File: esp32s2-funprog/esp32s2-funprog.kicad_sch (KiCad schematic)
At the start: 49 parts, among them J1 OPGM, J2 PGM, J3 USB_C_Receptacle_USB2.0, J4 MOUNT, J5 MOUNT, Q1 SE4625-PandN, Q2 SE4625-PandN, SW1 TS-1187A-B-A-B, U1 ESP32-S2, U2 AP1117-33, Y1 40MHz

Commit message: Update design per print.
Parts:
- removed D1, D2, D3: WS2816C-2121, cnhardware:WS2816-2121, symbol WS2816C:WS2816C-2121
- added D1, D2, D3: XL-1010RGBC-WS2812B, cnhardware:XL-1010RGBC-WS812B, symbol cnhardware:SK6805-EC15
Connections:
- net GND: now also D1.4 (GND), D2.4 (GND), D3.4 (GND)
- net VDD: now also D1.2 (VDD), D2.2 (VDD), D3.2 (VDD)
- net WSO: now also D1.1 (DI)
- new net: D1.3 (DO), D2.1 (DI)
- new net: D2.3 (DO), D3.1 (DI)

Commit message: Tweaks
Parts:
- added D5, D6, D7, D8, D9: XL-1010RGBC-WS2812B, cnhardware:XL-1010RGBC-WS812B, symbol cnhardware:SK6805-EC15
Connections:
- net GND: now also D5.4 (GND), D6.4 (GND), D7.4 (GND), D8.4 (GND), D9.4 (GND)
- net VDD: now also D5.2 (VDD), D6.2 (VDD), D7.2 (VDD), D8.2 (VDD), D9.2 (VDD)
- net at D3.3 (DO): now also D5.1 (DI)
- new net: D5.3 (DO), D6.1 (DI)
- new net: D6.3 (DO), D7.1 (DI)
- new net: D7.3 (DO), D8.1 (DI)
- new net: D8.3 (DO), D9.1 (DI)
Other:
- moved on the sheet: D1, D2, D3

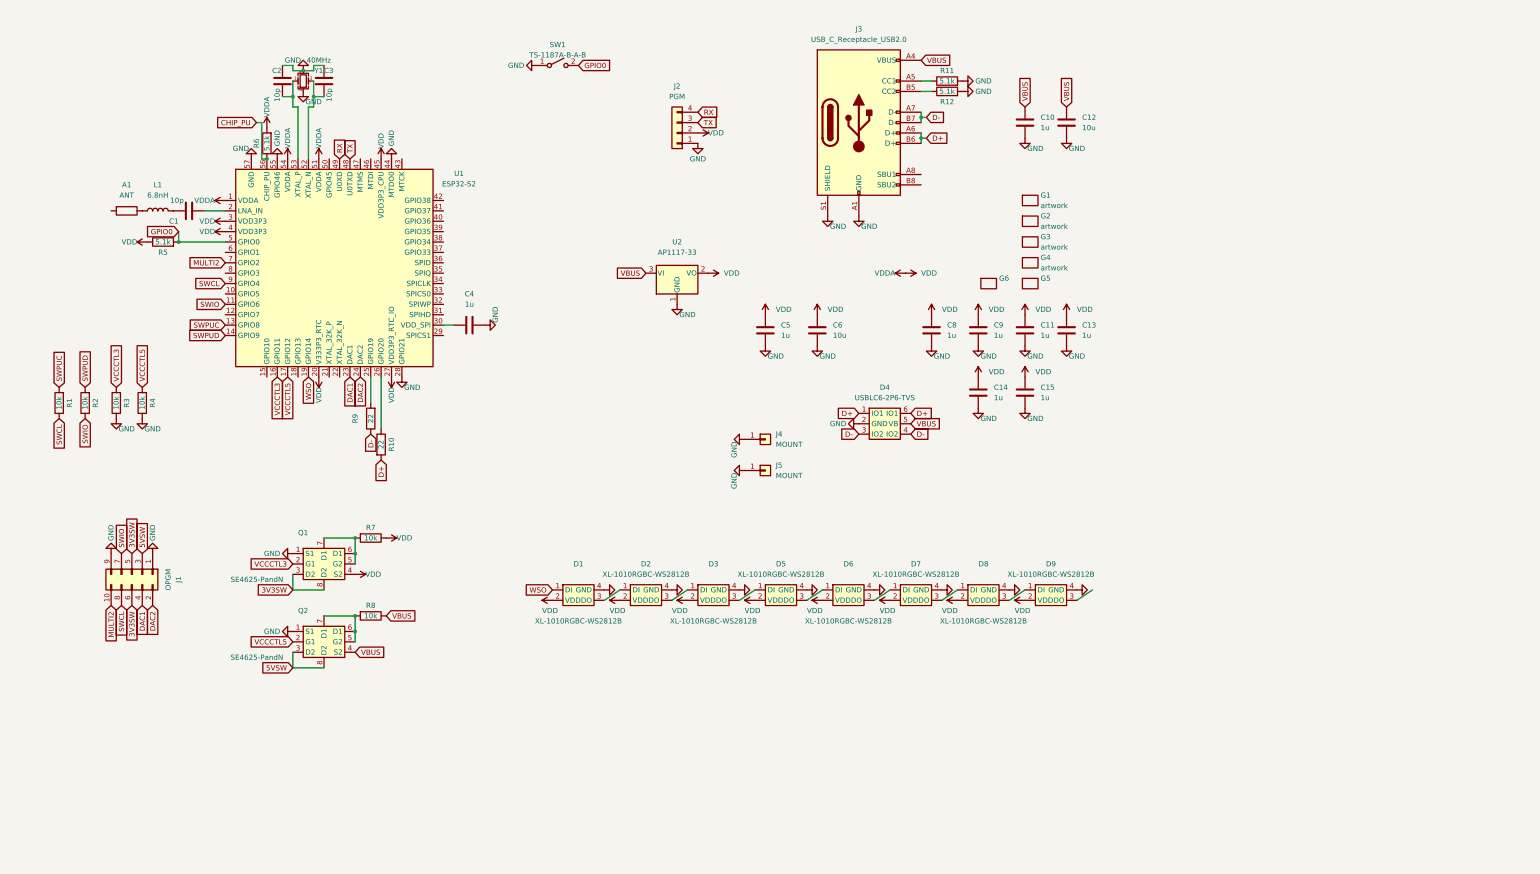
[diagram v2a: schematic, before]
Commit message: Maybe we can shoehorn it into the old programmer
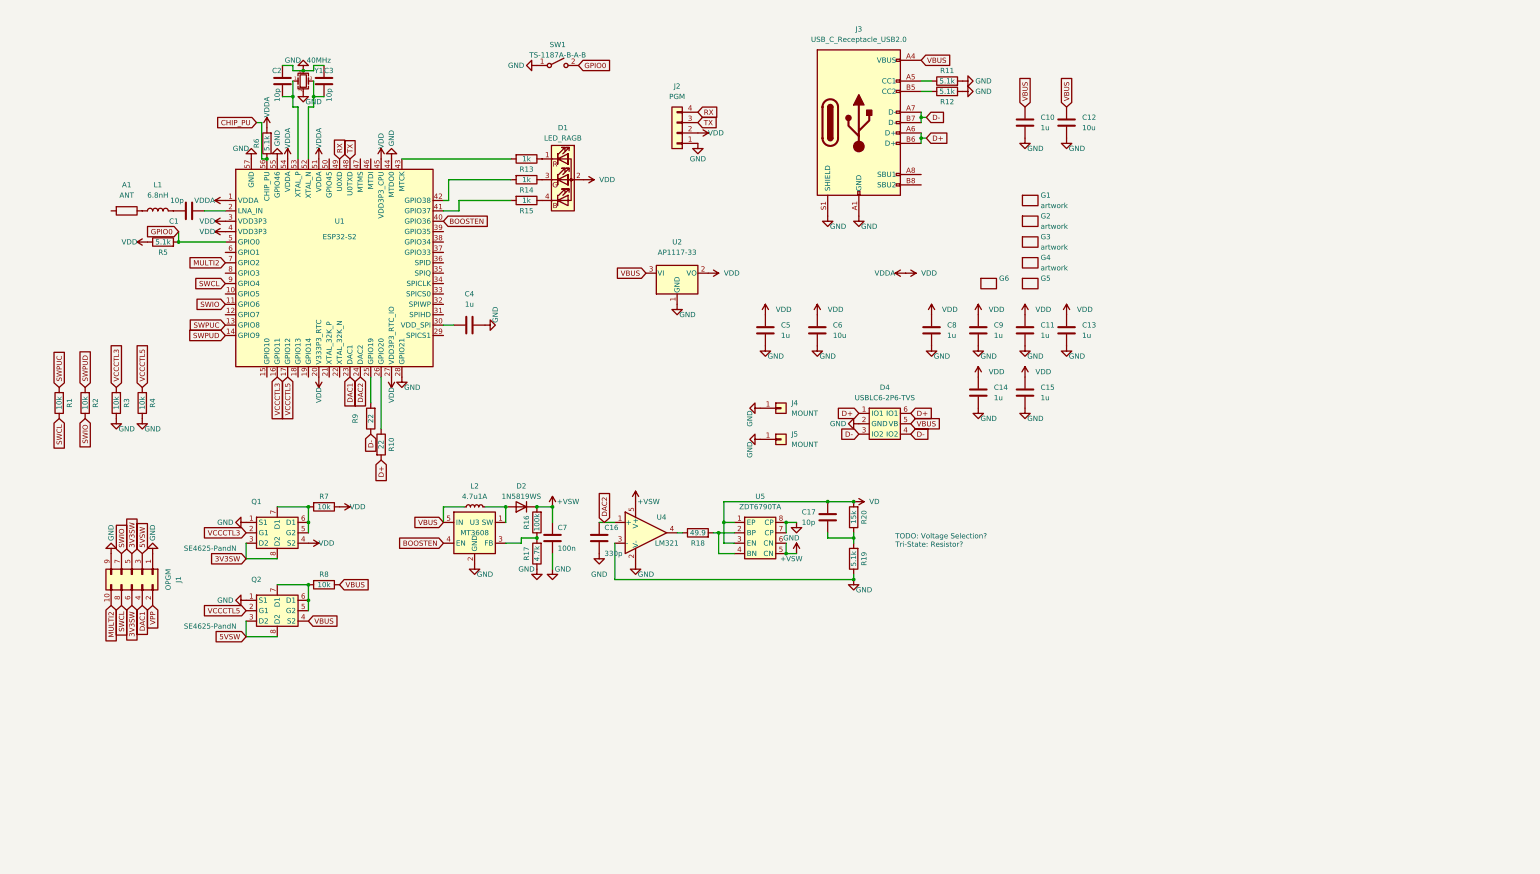
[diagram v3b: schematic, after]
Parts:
- removed D1, D2, D3, D5, D6, D7, D8, D9: XL-1010RGBC-WS2812B, cnhardware:XL-1010RGBC-WS812B, symbol cnhardware:SK6805-EC15
- added C16: 330p, Capacitor_SMD:C_0402_1005Metric, symbol Device:C
- added C17: 10p, Capacitor_SMD:C_0402_1005Metric, symbol Device:C
- added C7: 100n, Capacitor_SMD:C_0402_1005Metric, symbol Device:C
- added D1: LED_RAGB, LED_SMD:LED_WS2812B-2020_PLCC4_2.0x2.0mm, symbol Device:LED_RAGB
- added D2: 1N5819WS, Diode_SMD:D_SOD-323, symbol Device:D
- added L2: 4.7u1A, Inductor_SMD:L_1008_2520Metric, symbol Device:L_Small
- added R13, R14, R15: 1k, Resistor_SMD:R_0402_1005Metric, symbol Device:R
- added R16: 100k, Resistor_SMD:R_0402_1005Metric, symbol Device:R
- added R17: 4.7k, Resistor_SMD:R_0402_1005Metric, symbol Device:R
- added R18: 49.9, Resistor_SMD:R_0402_1005Metric, symbol Device:R
- added R19: 5.1k, Resistor_SMD:R_0402_1005Metric, symbol Device:R
- added R20: 15k, Resistor_SMD:R_0402_1005Metric, symbol Device:R
- added U3: MT3608, Package_TO_SOT_SMD:SOT-23-6, symbol Regulator_Switching:MT3608
- added U4: LM321, Package_TO_SOT_SMD:SOT-23-5, symbol Amplifier_Operational:LM321
- added U5: ZDT6790TA, Package_TO_SOT_SMD:SOT-223-8, symbol cnhardware:ZDT6790-COMPLEMENTARY-BJT
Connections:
- net DAC2: now also C16.1, U4.1 (+); no longer J1.2 (Pin_2)
- net GND: now also C16.2, C7.2, R17.1, R19.1, U3.2 (GND), U4.2 (V-), U4.3 (-), U5.7 (CP), U5.8 (CP)
- net VBUS: now also L2.1, U3.5 (IN)
- net VDD: now also D1.2 (A)
- net BOOSTEN: now reaches U1.40 (GPIO36)
- net BOOSTEN: now also U3.4 (EN)
- net at U1.41 (GPIO37): now also R15.2
- net at U1.42 (GPIO38): now also R14.2
- net at U1.43 (MTCK): now also R13.2
- net WSO: no longer names the net of U1.19 (GPIO14)
- new net: D2.2 (A), L2.2, U3.1 (SW)
- new net: C17.2, R19.2, R20.1
- new net: R16.1, R17.2, U3.3 (FB)
- new net: R18.1, U4.4
- new net: R18.2, U5.2 (BP), U5.4 (BN)
- new net: D1.1 (RK), R13.1
- new net: D1.3 (GK), R14.1
- new net: D1.4 (BK), R15.1
- new net +VSW: C7.1, D2.1 (K), R16.2, U4.5 (V+), U5.5 (CN), U5.6 (CN)
- new net VD: C17.1, R20.2, U5.1 (EP), U5.3 (EN)
- new net VPP: J1.2 (Pin_2)
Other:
- note added: "TODO: Voltage Selection? Tri-State: Resistor?"
- moved on the sheet: J4, J5, Q1, Q2, R7, R8

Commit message: Update design
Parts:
- added Q3: DWL336C, Package_TO_SOT_SMD:SOT-23-6, symbol cnhardware:DWL336C-P-AND-N
- added Q4, Q5: MOT2302, Package_TO_SOT_SMD:SOT-23, symbol Device:Q_NMOS_GDS
- added R21, R22: 10k, Resistor_SMD:R_0402_1005Metric, symbol Device:R
- added U6: COS4514, Package_TO_SOT_SMD:SOT-23-5, symbol cnhardware:COS4514-MUX-SPST
- added U8: HP3000, Package_DFN_QFN:DFN-8-1EP_2x2mm_P0.5mm_EP0.6x1.2mm, symbol cnhardware:HP3000-AD000-HD08R-DUAL-LOW-DRIVER
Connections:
- net +VSW: now also U6.5 (V+), U8.1 (ENA), U8.6 (VDD), U8.8 (ENB)
- net GND: now also Q3.5 (S1), Q4.3 (S), U6.3 (GND), U8.3 (GND), U8.9 (GND)
- net VD: now also Q3.2 (S2), Q5.2 (D), R21.1
- net VPP: now also Q3.4 (D2), Q3.6 (D1), Q5.3 (S), R22.2, U6.1 (COM)
- new net: Q3.3 (G2), U8.5 (OUTB)
- new net: Q3.1 (G1), U8.7 (OUTA)
- new net: Q4.2 (D), R22.1
- new net: R21.2, U6.2 (NO)
- new net VPPN2E: Q5.1 (G)
- new net VPPNEN: U8.2 (INA)
- new net VPPPD: Q4.1 (G)
- new net VPPPEN: U8.4 (INB)
- new net VPPUEN: U6.4 (IN)
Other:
- note added: "TODO: Primitive current monitoring? TODO: What if I want to drive output at very low voltages? Below VGSon for P fet in DWL, like 1.5V? No? Maybe another N fet?"
- moved on the sheet: R19, R20

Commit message: update with rev
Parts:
- removed Q5: MOT2302, Package_TO_SOT_SMD:SOT-23, symbol Device:Q_NMOS_GDS
- removed U2: AP1117-33, Package_TO_SOT_SMD:SOT-223-3_TabPin2, symbol Regulator_Linear:AP1117-33
- removed U4: LM321, Package_TO_SOT_SMD:SOT-23-5, symbol Amplifier_Operational:LM321
- removed U5: ZDT6790TA, Package_TO_SOT_SMD:SOT-223-8, symbol cnhardware:ZDT6790-COMPLEMENTARY-BJT
- removed U6: COS4514, Package_TO_SOT_SMD:SOT-23-5, symbol cnhardware:COS4514-MUX-SPST
- added C18, C22: 100n, Capacitor_SMD:C_0402_1005Metric, symbol Device:C
- added C19: 330p, Capacitor_SMD:C_0402_1005Metric, symbol Device:C
- added C20, C21, C23, C24: 10p, Capacitor_SMD:C_0402_1005Metric, symbol Device:C
- added C25: 10u, Capacitor_SMD:C_0603_1608Metric, symbol Device:C
- added C26: 1u, Capacitor_SMD:C_0402_1005Metric, symbol Device:C
- added Q6: 2N7002KDW, Package_TO_SOT_SMD:SOT-363_SC-70-6, symbol cnhardware:DWL336C-P-AND-N
- added Q7: MOT2302, Package_TO_SOT_SMD:SOT-23, symbol Device:Q_NMOS_GDS
- added R23: 12k, Resistor_SMD:R_0402_1005Metric, symbol Device:R
- added R24: 2.2k, Resistor_SMD:R_0402_1005Metric, symbol Device:R
- added R25: 49.9, Resistor_SMD:R_0402_1005Metric, symbol Device:R
- added R26: 15k, Resistor_SMD:R_0402_1005Metric, symbol Device:R
- added R27: 5.1k, Resistor_SMD:R_0402_1005Metric, symbol Device:R
- added R28, R29, R30, R31: 10k, Resistor_SMD:R_0402_1005Metric, symbol Device:R
- added U10: LM321, Package_TO_SOT_SMD:SOT-23-5, symbol Amplifier_Operational:LM321
- added U11: ZDT6790TA, Package_TO_SOT_SMD:SOT-223-8, symbol cnhardware:ZDT6790-COMPLEMENTARY-BJT
- added U12: COS4514, Package_TO_SOT_SMD:SOT-23-5, symbol cnhardware:COS4514-MUX-SPST
- added U13: ~, Package_DFN_QFN:DFN-8-1EP_3x3mm_P0.5mm_EP1.65x2.38mm, symbol cnhardware:NCP81155-GATE-DRIVER
- added U14, U15, U16, U9: AT8837, Package_DFN_QFN:DFN-8-1EP_2x2mm_P0.45mm_EP0.64x1.38mm, symbol cnhardware:BDR6122TC-MOTOR-DRIVER
- added U2, U4, U6: XC6206P332, Package_TO_SOT_SMD:SOT-23, symbol Regulator_Linear:IFX27001TFV26
- added U5: COSNE5532, Package_SO:MSOP-8_3x3mm_P0.65mm, symbol cnhardware:LM2903-SOIC8
- C14, C15: value 1u -> 10p; LCSC C106254 -> C106199
- C16: value 330p -> 1u; LCSC C13533 -> C106254
- C2, C3: value 10p -> 2.2p; LCSC C106199 -> C1559
- L2: value 4.7u1A -> 4.7u500mA; footprint Inductor_SMD:L_1008_2520Metric -> Inductor_SMD:L_0805_2012Metric; LCSC C98340 -> C63166
- Q3, U8: now not fitted; now left out of the parts list
- Q4: value MOT2302 -> 2N7002; LCSC C5143129 -> C8545
- R13, R14, R15: value 1k -> 510; LCSC C102748 -> C25123
- R16: value 100k -> 510; LCSC C25741 -> C25123
- R17: value 4.7k -> 2.2k; LCSC C25900 -> C25879
- R18: value 49.9 -> 2.2k; LCSC C25120 -> C25879
- R19: value 5.1k -> 15k; LCSC C105872 -> C25756
- R20: value 15k -> 5.1k; LCSC C25756 -> C105872
- R21: value 10k -> 15k; LCSC C144807 -> C25756
- R22: value 10k -> 5.1k; LCSC C144807 -> C105872
- U3: footprint Package_TO_SOT_SMD:SOT-23-6 -> Package_TO_SOT_SMD:SOT-23-5
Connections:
- net +VSW: now also C25.1, R23.2, U10.5 (V+), U11.5 (CN), U11.6 (CN), U12.5 (V+), U13.1 (BST), U15.1 (VM), U16.1 (VM), U5.8 (Vcc); no longer R16.2
- net 3V3SW: no longer J1.6 (Pin_6)
- net BOOSTEN: now also U1.43 (MTCK); no longer U1.40 (GPIO36)
- net DAC1: now also C14.2, C19.1, U10.1 (+), U5.3 (I1+); no longer J1.4 (Pin_4)
- net DAC2: now also C15.2, U5.5 (I2+); no longer C16.1
- net GND: now also C14.1, C15.1, R16.1, R20.1, R22.1, C18.2, C19.2, C22.2, C23.2, C24.2, C25.2, C26.1, Q6.4 (D2), Q7.3 (S), R27.1, U10.2 (V-), U11.7 (CP), U11.8 (CP), U12.3 (GND), U13.6 (GND), U13.9 (GND), U14.4 (GND), U14.9 (FLAG), U15.4 (GND), U15.9 (FLAG), U16.4 (GND), U16.9 (FLAG), U2.1 (GND), U4.1 (GND), U5.4 (GND), U6.1 (GND), U9.4 (GND), U9.9 (FLAG); no longer C14.2, C15.2, R17.1, R19.1
- net MULTI2: now also J1.6 (Pin_6); no longer J1.10 (Pin_10)
- net VBUS: now also C26.2, U13.4 (VCC), U2.3 (I), U4.3 (I), U6.3 (I)
- net VCCCTL3: now also U1.10 (GPIO5); no longer U1.16 (GPIO11)
- net VCCCTL5: now also U1.8 (GPIO3); no longer U1.17 (GPIO12)
- net VD: now also Q6.6 (D1), R28.1; no longer C17.1, R20.2, R21.1
- net VDD: now also R18.1, U14.6 (IN1), U14.8 (VCC), U15.6 (IN1), U15.8 (VCC), U16.6 (IN1), U16.8 (VCC), U4.2 (Q), U9.6 (IN1), U9.8 (VCC); no longer C14.1, C15.1, Q1.4 (S2), R7.1, U1.20 (V333P3_RTC)
- net VPP: now also U12.1 (COM); no longer J1.2 (Pin_2), R22.2
- net VPI1: now reaches Q4.2 (D)
- net VPI1: now also R18.2, U1.19 (GPIO14); no longer R22.1
- net at R17.2, U3.3 (FB): now also R16.2, R23.1; no longer R16.1
- net VD2: now reaches R21.2
- net VD2: now also J1.4 (Pin_4), C21.1, C23.1, U5.7 (O2)
- net OPEN1: now reaches U1.18 (GPIO13)
- net OPEN1: now also U14.7 (nSLP)
- net at R15.2: now also D1.4 (BK); no longer U1.41 (GPIO37)
- net at R14.2: now also D1.3 (GK); no longer U1.42 (GPIO38)
- net at R13.2: now also D1.1 (RK); no longer U1.43 (MTCK)
- net at U1.46 (MTDI): now also R14.1
- net at U1.47 (MTMS): now also R15.1
- net at U1.50 (GPIO45): now also R13.1
- net MULTI1: now reaches U1.6 (GPIO1)
- net MULTI1: now also J1.10 (Pin_10)
- net VPPNEN: no longer names the net of U8.2 (INA)
- net VPPPD renamed VPP1
- net VPP1: now also J1.2 (Pin_2), Q6.2 (S2), Q6.5 (S1), R29.2, R30.2, U13.7 (SW), U9.2 (OUT1)
- net VPPPEN: no longer names the net of U8.4 (INB)
- new net: R30.1, U14.2 (OUT1)
- new net: Q1.4 (S2), R7.1, U6.2 (Q)
- new net: Q7.2 (D), R29.1
- new net: C20.2, R26.1, R27.2, U10.3 (-)
- new net: R31.1, U16.2 (OUT1)
- new net: R25.2, U11.2 (BP), U11.4 (BN)
- new net: R28.2, U12.2 (NO)
- new net: Q6.3 (G2), U13.5 (DL)
- new net: Q6.1 (G1), U13.8 (DH)
- new net: C18.1, R17.1, R24.1
- new net: R25.1, U10.4
- new net BOOSTV: R24.2, U1.42 (GPIO38)
- new net D1OEN: U13.3 (EN)
- new net D1OV: U13.2 (PWM)
- new net D1PDEN: Q7.1 (G)
- new net D1PUEN: U12.4 (IN)
- new net OD1: U1.16 (GPIO11), U14.5 (IN2), U9.5 (IN2)
- new net OD2: U15.5 (IN2), U16.5 (IN2)
- new net OEN1: U1.17 (GPIO12), U9.7 (nSLP)
- new net OEN2: U15.7 (nSLP)
- new net OPEN2: U16.7 (nSLP)
- new net V1FB: C17.2, R19.1, R20.2, U5.2 (I1-)
- new net V2FB: C21.2, R21.1, R22.2, U5.6 (I2-)
- new net VD1: C17.1, C20.1, C22.1, C24.1, R19.2, R26.2, U11.1 (EP), U11.3 (EN), U14.1 (VM), U5.1 (O1), U9.1 (VM)
- new net VDDA: C16.1, U1.20 (V333P3_RTC), U2.2 (Q)
- new net VPP2: R31.2, U15.2 (OUT1)
- no-connect marks 0 -> 4
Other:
- note added: "+VST may be 7.5 to 16.6V"
- note added: "TODO: Evaluate C14/C15, C17, C21 C2, C3"
- note removed: "TODO: Voltage Selection? Tri-State: Resistor?"
- moved on the sheet: C11, C13, C5, C6, C7, C8, C9, D2, D4, G6, J1, J3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

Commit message: Update fixing 6-pin pinout
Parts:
- U3: footprint Package_TO_SOT_SMD:SOT-23-5 -> Package_TO_SOT_SMD:SOT-23-6
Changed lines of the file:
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@@
       (effects (font (size 1.27 1.27)))
     )
-    (property "Footprint" "Package_TO_SOT_SMD:SOT-23-5" (at 149.86 149.86 0)
+    (property "Footprint" "Package_TO_SOT_SMD:SOT-23-6" (at 149.86 149.86 0)
       (effects (font (size 1.27 1.27) italic) (justify left) hide)
     )

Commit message: Bump - back to legacy
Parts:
- removed C16, C26: 1u, Capacitor_SMD:C_0402_1005Metric, symbol Device:C
- removed C17, C20, C21, C23, C24: 10p, Capacitor_SMD:C_0402_1005Metric, symbol Device:C
- removed C18, C22, C7: 100n, Capacitor_SMD:C_0402_1005Metric, symbol Device:C
- removed C19: 330p, Capacitor_SMD:C_0402_1005Metric, symbol Device:C
- removed C25: 10u, Capacitor_SMD:C_0603_1608Metric, symbol Device:C
- removed D1: LED_RAGB, LED_SMD:LED_WS2812B-2020_PLCC4_2.0x2.0mm, symbol Device:LED_RAGB
- removed D2: 1N5819WS, Diode_SMD:D_SOD-323, symbol Device:D
- removed L2: 4.7u500mA, Inductor_SMD:L_0805_2012Metric, symbol Device:L_Small
- removed Q3: DWL336C, Package_TO_SOT_SMD:SOT-23-6, symbol cnhardware:DWL336C-P-AND-N
- removed Q4: 2N7002, Package_TO_SOT_SMD:SOT-23, symbol Device:Q_NMOS_GDS
- removed Q6: 2N7002KDW, Package_TO_SOT_SMD:SOT-363_SC-70-6, symbol cnhardware:DWL336C-P-AND-N
- removed Q7: MOT2302, Package_TO_SOT_SMD:SOT-23, symbol Device:Q_NMOS_GDS
- removed R13, R14, R15, R16: 510, Resistor_SMD:R_0402_1005Metric, symbol Device:R
- removed R17, R18, R24: 2.2k, Resistor_SMD:R_0402_1005Metric, symbol Device:R
- removed R19, R21, R26: 15k, Resistor_SMD:R_0402_1005Metric, symbol Device:R
- removed R20, R22, R27: 5.1k, Resistor_SMD:R_0402_1005Metric, symbol Device:R
- removed R23: 12k, Resistor_SMD:R_0402_1005Metric, symbol Device:R
- removed R25: 49.9, Resistor_SMD:R_0402_1005Metric, symbol Device:R
- removed R28, R29, R30, R31: 10k, Resistor_SMD:R_0402_1005Metric, symbol Device:R
- removed U10: LM321, Package_TO_SOT_SMD:SOT-23-5, symbol Amplifier_Operational:LM321
- removed U11: ZDT6790TA, Package_TO_SOT_SMD:SOT-223-8, symbol cnhardware:ZDT6790-COMPLEMENTARY-BJT
- removed U12: COS4514, Package_TO_SOT_SMD:SOT-23-5, symbol cnhardware:COS4514-MUX-SPST
- removed U13: ~, Package_DFN_QFN:DFN-8-1EP_3x3mm_P0.5mm_EP1.65x2.38mm, symbol cnhardware:NCP81155-GATE-DRIVER
- removed U14, U15, U16, U9: AT8837, Package_DFN_QFN:DFN-8-1EP_2x2mm_P0.45mm_EP0.64x1.38mm, symbol cnhardware:BDR6122TC-MOTOR-DRIVER
- removed U2, U4, U6: XC6206P332, Package_TO_SOT_SMD:SOT-23, symbol Regulator_Linear:IFX27001TFV26
- removed U3: MT3608, Package_TO_SOT_SMD:SOT-23-6, symbol Regulator_Switching:MT3608
- removed U5: COSNE5532, Package_SO:MSOP-8_3x3mm_P0.65mm, symbol cnhardware:LM2903-SOIC8
- removed U8: HP3000, Package_DFN_QFN:DFN-8-1EP_2x2mm_P0.5mm_EP0.6x1.2mm, symbol cnhardware:HP3000-AD000-HD08R-DUAL-LOW-DRIVER
- added D1, D2, D3, D5, D6, D7, D8, D9: XL-1010RGBC-WS2812B, cnhardware:XL-1010RGBC-WS812B, symbol cnhardware:SK6805-EC15
- added U2: AP1117-33, Package_TO_SOT_SMD:SOT-223-3_TabPin2, symbol Regulator_Linear:AP1117-33
- C14, C15: value 10p -> 1u; LCSC C106199 -> C106254
- C2, C3: value 2.2p -> 10p; LCSC C1559 -> C106199
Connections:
- net OD1 is gone; now on net VCCCTL3: U1.16 (GPIO11)
- net OEN1 is gone; now on net VCCCTL5: U1.17 (GPIO12)
- net VD2 is gone; now on net DAC1: J1.4 (Pin_4)
- net VDDA is gone; now on net VDD: U1.20 (V333P3_RTC)
- net VPP1 is gone; now on net DAC2: J1.2 (Pin_2)
- net 3V3SW: now also J1.6 (Pin_6)
- net DAC1: no longer C14.2
- net DAC2: no longer C15.2
- net GND: now also C14.2, C15.2, D1.4 (GND), D2.4 (GND), D3.4 (GND), D5.4 (GND), D6.4 (GND), D7.4 (GND), D8.4 (GND), D9.4 (GND), U2.1 (GND); no longer C14.1, C15.1
- net MULTI2: now also J1.10 (Pin_10); no longer J1.6 (Pin_6)
- net VBUS: now also U2.3 (VI)
- net VCCCTL3: no longer U1.10 (GPIO5)
- net VCCCTL5: no longer U1.8 (GPIO3)
- net VDD: now also C14.1, C15.1, Q1.4 (S2), R7.1, D1.2 (VDD), D2.2 (VDD), D3.2 (VDD), D5.2 (VDD), D6.2 (VDD), D7.2 (VDD), D8.2 (VDD), D9.2 (VDD), U2.2 (VO)
- net BOOSTEN: no longer names the net of U1.43 (MTCK)
- net BOOSTV: no longer names the net of U1.42 (GPIO38)
- net MULTI1: no longer names the net of U1.6 (GPIO1)
- net MULTI1: no longer J1.10 (Pin_10)
- net OPEN1: no longer names the net of U1.18 (GPIO13)
- net VPI1 renamed WSO
- net WSO: now also D1.1 (DI)
- new net: D5.3 (DO), D6.1 (DI)
- new net: D6.3 (DO), D7.1 (DI)
- new net: D3.3 (DO), D5.1 (DI)
- new net: D7.3 (DO), D8.1 (DI)
- new net: D1.3 (DO), D2.1 (DI)
- new net: D2.3 (DO), D3.1 (DI)
- new net: D8.3 (DO), D9.1 (DI)
- no-connect marks 4 -> 0
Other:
- note removed: "+VST may be 7.5 to 16.6V"
- note removed: "TODO: Evaluate C14/C15, C17, C21 C2, C3"
- note removed: "TODO: Primitive current monitoring? TODO: What if I want to drive output at very low voltages? Below VGSon for P fet in DWL, like 1.5V? No? Maybe another N fet?"
- moved on the sheet: C11, C13, C5, C6, C8, C9, D4, G6, J1, J3, J4, J5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
